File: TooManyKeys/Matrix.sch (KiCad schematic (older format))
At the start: 222 parts

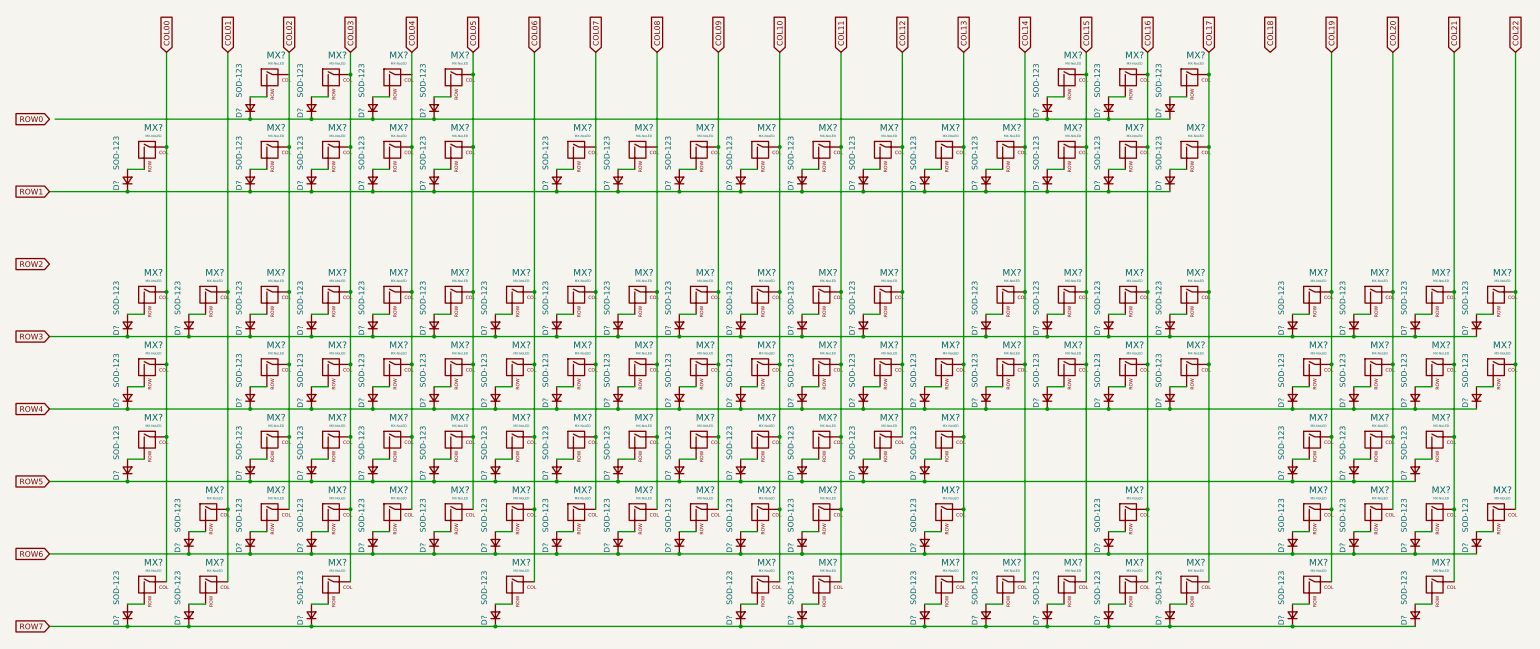
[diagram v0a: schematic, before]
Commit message: adding voltage controller and i2c controller
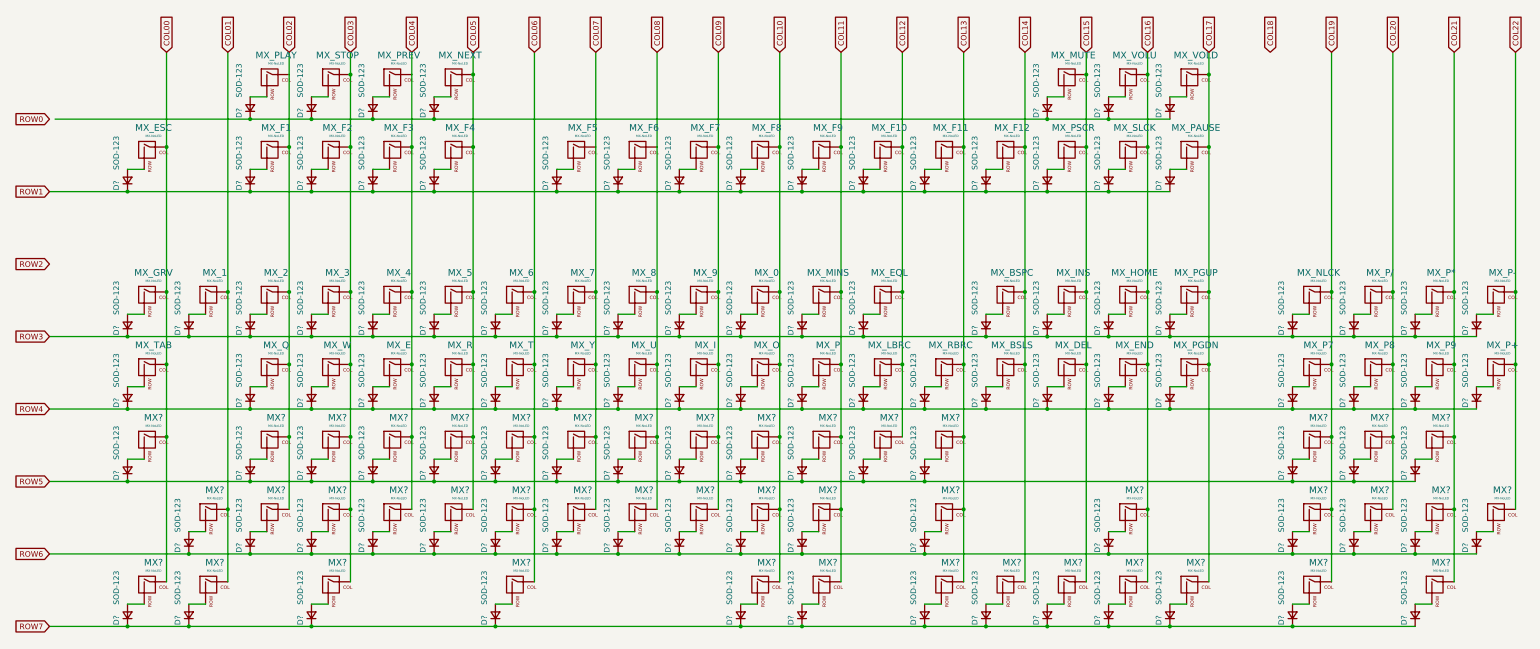
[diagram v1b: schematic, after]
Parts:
- gave numbers to parts that had none: 65

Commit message: finish work on matrix
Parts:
- gave numbers to parts that had none: 46

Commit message: WIP pcb
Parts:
- D1, D10, D100, D101, D102, D103, D104, D105, D106, D107, D108, D109, D11, D110, D111, D12, D13, D14, D15, D16, D17, D18, D19, D2, D20, D21, D22, D23, D24, D25, D26, D27, D28, D29, D3, D30, D31, D32, D33, D34, D35, D36, D37, D38, D39, D4, D40, D41, D42, D43, D44, D45, D46, D47, D48, D49, D5, D50, D51, D52, D53, D54, D55, D56, D57, D58, D59, D6, D60, D61, D62, D63, D64, D65, D66, D67, D68, D69, D7, D70, D71, D72, D73, D74, D75, D76, D77, D78, D79, D8, D80, D81, D82, D83, D84, D85, D86, D87, D88, D89, D9, D90, D91, D92, D93, D94, D95, D96, D97, D98, D99: renamed from D?; footprint (none) -> Diode_SMD:D_SOD-123
- MX_0, MX_1, MX_2, MX_3, MX_4, MX_5, MX_6, MX_7, MX_8, MX_9, MX_F1, MX_F10, MX_F11, MX_F12, MX_F2, MX_F3, MX_F4, MX_F5, MX_F6, MX_F7, MX_F8, MX_F9, MX_P1, MX_P2, MX_P3, MX_P4, MX_P5, MX_P6, MX_P7, MX_P8, MX_P9: footprint (none) -> MX_Only:MXOnly-1U-NoLED
- MX_A1: renamed from MX_A; footprint (none) -> MX_Only:MXOnly-1U-NoLED
- MX_B1: renamed from MX_B; footprint (none) -> MX_Only:MXOnly-1U-NoLED
- MX_BSLS1: renamed from MX_BSLS; footprint (none) -> MX_Only:MXOnly-1.5U-NoLED
- MX_BSPC1: renamed from MX_BSPC; footprint (none) -> MX_Only:MXOnly-2U-NoLED
- MX_C1: renamed from MX_C; footprint (none) -> MX_Only:MXOnly-1U-NoLED
- MX_CAPS1: renamed from MX_CAPS; footprint (none) -> MX_Only:MXOnly-1.75U-NoLED
- MX_COMM1: renamed from MX_COMM; footprint (none) -> MX_Only:MXOnly-1U-NoLED
- MX_D1: renamed from MX_D; footprint (none) -> MX_Only:MXOnly-1U-NoLED
- MX_DEL1: renamed from MX_DEL; footprint (none) -> MX_Only:MXOnly-1U-NoLED
- MX_DOT1: renamed from MX_DOT; footprint (none) -> MX_Only:MXOnly-1U-NoLED
- MX_DOWN1: renamed from MX_DOWN; footprint (none) -> MX_Only:MXOnly-1U-NoLED
- MX_E1: renamed from MX_E; footprint (none) -> MX_Only:MXOnly-1U-NoLED
- MX_END1: renamed from MX_END; footprint (none) -> MX_Only:MXOnly-1U-NoLED
- MX_ENT1: renamed from MX_ENT; footprint (none) -> MX_Only:MXOnly-2.25U-NoLED
- MX_EQL1: renamed from MX_EQL; footprint (none) -> MX_Only:MXOnly-1U-NoLED
- MX_ESC1: renamed from MX_ESC; footprint (none) -> MX_Only:MXOnly-1U-NoLED
- MX_F13: renamed from MX_F; footprint (none) -> MX_Only:MXOnly-1U-NoLED
- MX_G1: renamed from MX_G; footprint (none) -> MX_Only:MXOnly-1U-NoLED
- MX_GRV1: renamed from MX_GRV; footprint (none) -> MX_Only:MXOnly-1U-NoLED
- MX_H1: renamed from MX_H; footprint (none) -> MX_Only:MXOnly-1U-NoLED
- MX_HOME1: renamed from MX_HOME; footprint (none) -> MX_Only:MXOnly-1U-NoLED
- MX_I1: renamed from MX_I; footprint (none) -> MX_Only:MXOnly-1U-NoLED
- MX_INS1: renamed from MX_INS; footprint (none) -> MX_Only:MXOnly-1U-NoLED
- MX_J1: renamed from MX_J; footprint (none) -> MX_Only:MXOnly-1U-NoLED
- MX_K1: renamed from MX_K; footprint (none) -> MX_Only:MXOnly-1U-NoLED
- MX_L1: renamed from MX_L; footprint (none) -> MX_Only:MXOnly-1U-NoLED
- MX_LALT1: renamed from MX_LALT; footprint (none) -> MX_Only:MXOnly-1.25U-NoLED
- MX_LBRC1: renamed from MX_LBRC; footprint (none) -> MX_Only:MXOnly-1U-NoLED
- MX_LCTL1: renamed from MX_LCTL; footprint (none) -> MX_Only:MXOnly-1.25U-NoLED
- MX_LEFT1: renamed from MX_LEFT; footprint (none) -> MX_Only:MXOnly-1U-NoLED
- MX_LGUI1: renamed from MX_LGUI; footprint (none) -> MX_Only:MXOnly-1.25U-NoLED
- MX_LSFT1: renamed from MX_LSFT; footprint (none) -> MX_Only:MXOnly-2.25U-NoLED
- MX_M1: renamed from MX_M; footprint (none) -> MX_Only:MXOnly-1U-NoLED
- MX_MENU1: renamed from MX_MENU; footprint (none) -> MX_Only:MXOnly-1.25U-NoLED
- MX_MINS1: renamed from MX_MINS; footprint (none) -> MX_Only:MXOnly-1U-NoLED
- MX_MUTE1: renamed from MX_MUTE; footprint (none) -> MX_Only:MXOnly-1U-NoLED
- MX_N1: renamed from MX_N; footprint (none) -> MX_Only:MXOnly-1U-NoLED
- MX_NEXT1: renamed from MX_NEXT; footprint (none) -> MX_Only:MXOnly-1U-NoLED
- MX_NLCK1: renamed from MX_NLCK; footprint (none) -> MX_Only:MXOnly-1U-NoLED
- MX_O1: renamed from MX_O; footprint (none) -> MX_Only:MXOnly-1U-NoLED
- MX_P*1: renamed from MX_P*; footprint (none) -> MX_Only:MXOnly-1U-NoLED
- MX_P+1: renamed from MX_P+; footprint (none) -> MX_Only:MXOnly-2U-NoLED
- MX_P-1: renamed from MX_P-; footprint (none) -> MX_Only:MXOnly-1U-NoLED
- MX_P/1: renamed from MX_P/; footprint (none) -> MX_Only:MXOnly-1U-NoLED
- MX_P0: footprint (none) -> MX_Only:MXOnly-2U-NoLED
- MX_P10: renamed from MX_P; footprint (none) -> MX_Only:MXOnly-1U-NoLED
- MX_PAUSE1: renamed from MX_PAUSE; footprint (none) -> MX_Only:MXOnly-1U-NoLED
- MX_PDOT1: renamed from MX_PDOT; footprint (none) -> MX_Only:MXOnly-1U-NoLED
- MX_PENT1: renamed from MX_PENT; footprint (none) -> MX_Only:MXOnly-2U-NoLED
- MX_PGDN1: renamed from MX_PGDN; footprint (none) -> MX_Only:MXOnly-1U-NoLED
- MX_PGUP1: renamed from MX_PGUP; footprint (none) -> MX_Only:MXOnly-1U-NoLED
- MX_PLAY1: renamed from MX_PLAY; footprint (none) -> MX_Only:MXOnly-1U-NoLED
- MX_PREV1: renamed from MX_PREV; footprint (none) -> MX_Only:MXOnly-1U-NoLED
- MX_PSCR1: renamed from MX_PSCR; footprint (none) -> MX_Only:MXOnly-1U-NoLED
- MX_Q1: renamed from MX_Q; footprint (none) -> MX_Only:MXOnly-1U-NoLED
- MX_QUOT1: renamed from MX_QUOT; footprint (none) -> MX_Only:MXOnly-1U-NoLED
- MX_R1: renamed from MX_R; footprint (none) -> MX_Only:MXOnly-1U-NoLED
- MX_RALT1: renamed from MX_RALT; footprint (none) -> MX_Only:MXOnly-1.25U-NoLED
- MX_RBRC1: renamed from MX_RBRC; footprint (none) -> MX_Only:MXOnly-1U-NoLED
- MX_RCTL1: renamed from MX_RCTL; footprint (none) -> MX_Only:MXOnly-1U-NoLED
- MX_RGHT1: renamed from MX_RGHT; footprint (none) -> MX_Only:MXOnly-1.25U-NoLED
- MX_RGUI1: renamed from MX_RGUI; footprint (none) -> MX_Only:MXOnly-1.25U-NoLED
- MX_RSFT1: renamed from MX_RSFT; footprint (none) -> MX_Only:MXOnly-2.75U-NoLED
- MX_S1: renamed from MX_S; footprint (none) -> MX_Only:MXOnly-1U-NoLED
- MX_SCLN1: renamed from MX_SCLN; footprint (none) -> MX_Only:MXOnly-1U-NoLED
- MX_SLCK1: renamed from MX_SLCK; footprint (none) -> MX_Only:MXOnly-1U-NoLED
- MX_SLSH1: renamed from MX_SLSH; footprint (none) -> MX_Only:MXOnly-1U-NoLED
- MX_SPC1: renamed from MX_SPC; footprint (none) -> MX_Only:MXOnly-6.25U-NoLED
- MX_STOP1: renamed from MX_STOP; footprint (none) -> MX_Only:MXOnly-1U-NoLED
- MX_T1: renamed from MX_T; footprint (none) -> MX_Only:MXOnly-1U-NoLED
- MX_TAB1: renamed from MX_TAB; footprint (none) -> MX_Only:MXOnly-1.5U-NoLED
- MX_U1: renamed from MX_U; footprint (none) -> MX_Only:MXOnly-1U-NoLED
- MX_UP1: renamed from MX_UP; footprint (none) -> MX_Only:MXOnly-1U-NoLED
- MX_V1: renamed from MX_V; footprint (none) -> MX_Only:MXOnly-1U-NoLED
- MX_VOLD1: renamed from MX_VOLU; footprint (none) -> MX_Only:MXOnly-1U-NoLED
- MX_VOLU1: renamed from MX_VOLD; footprint (none) -> MX_Only:MXOnly-1U-NoLED
- MX_W1: renamed from MX_W; footprint (none) -> MX_Only:MXOnly-1U-NoLED
- MX_X1: renamed from MX_X; footprint (none) -> MX_Only:MXOnly-1U-NoLED
- MX_Y1: renamed from MX_Y; footprint (none) -> MX_Only:MXOnly-1U-NoLED
- MX_Z1: renamed from MX_Z; footprint (none) -> MX_Only:MXOnly-1U-NoLED
